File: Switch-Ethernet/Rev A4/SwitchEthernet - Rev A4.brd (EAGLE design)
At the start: 86 x 90 mm, 118 parts, among them J1 22-05-7028-02, J2 DF17(2.0)-20DP-0.5V(57), J3 DF17(4.0)-20DP-0.5V(57), J4 22-05-7058-05, P1 RB1-125BAG1A, T1 H1102FNL, T2 H1102FNL, U1 TC1264-3.3, U2 TC1264-1.8, U3 KSZ8995MA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

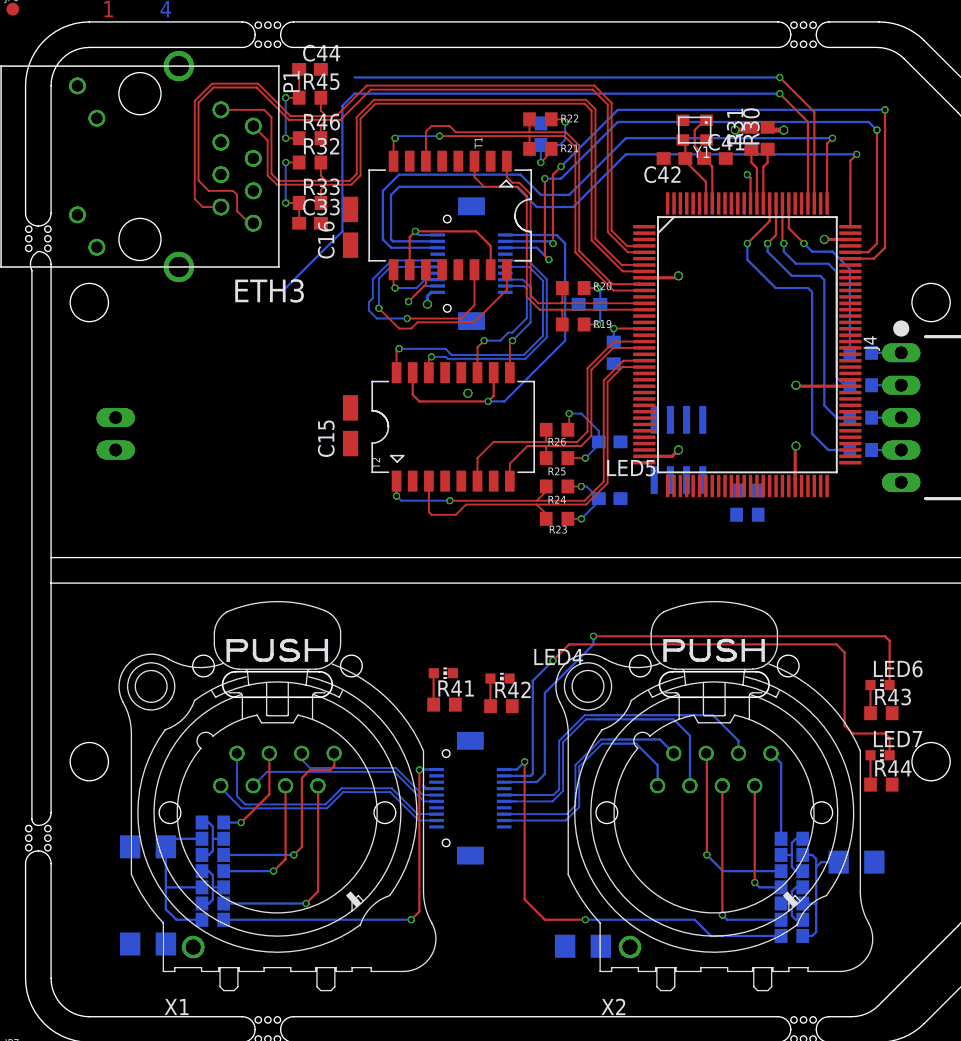
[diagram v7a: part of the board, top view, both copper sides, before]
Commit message: change position of the resistors of neutrix connectors and re-route
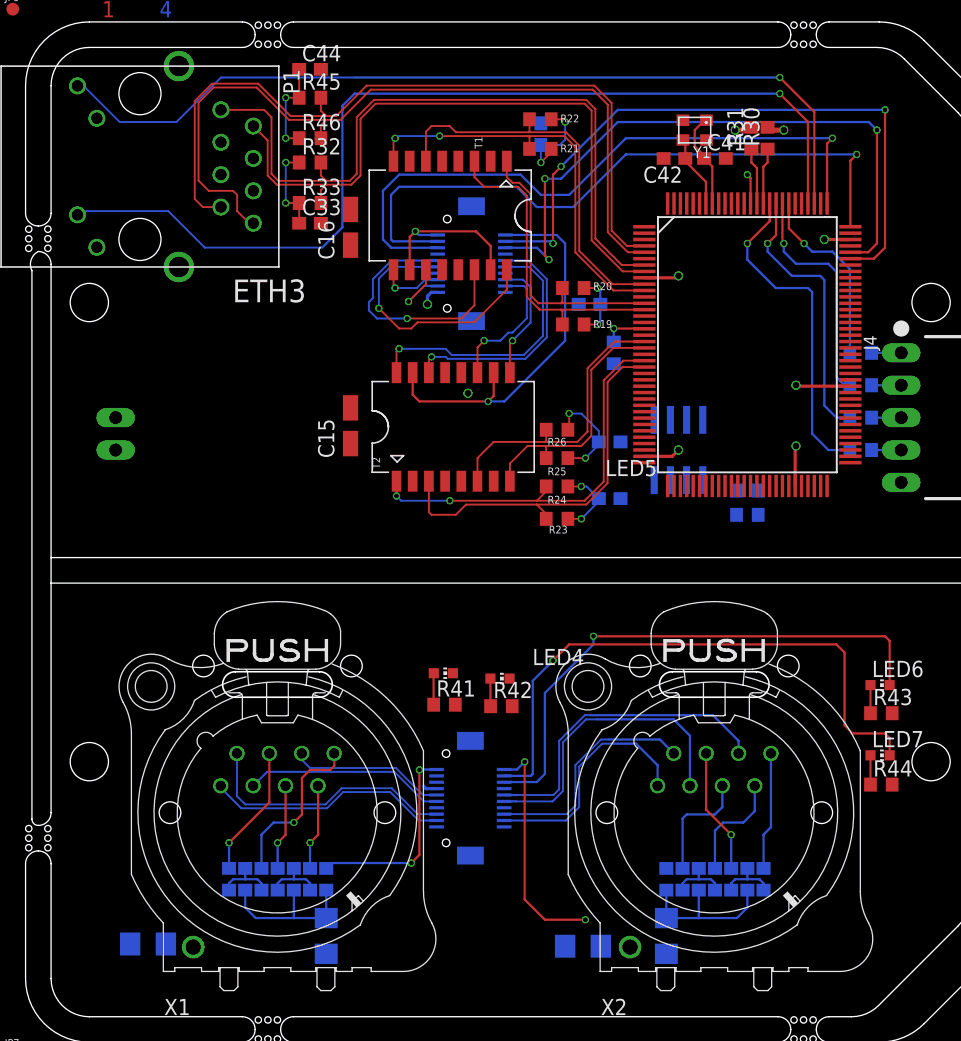
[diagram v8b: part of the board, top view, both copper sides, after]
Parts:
- moved C11 16.0 mm to (55.2, 13.3), turned to 270 degrees
- moved C12 15.6 mm to (28.6, 13.3), turned to 270 degrees
- moved R13 10.8 mm to (55.2, 17.8), turned to 90 degrees
- moved R6 9.44 mm to (28.6, 17.8), turned to 90 degrees
- moved R14 9.14 mm to (56.5, 17.8), turned to 90 degrees
- moved R8 7.85 mm to (27.3, 17.8), turned to 90 degrees
- moved R15 7.55 mm to (57.8, 17.8), turned to 90 degrees
- moved R18 6.38 mm to (26.0, 17.8), turned to 90 degrees
- moved R12 6.07 mm to (59.1, 17.8), turned to 90 degrees
- moved R17 5.12 mm to (24.8, 17.8), turned to 90 degrees
- moved R16 4.80 mm to (60.3, 17.8), turned to 90 degrees
- moved R11 4.62 mm to (21.0, 17.8), turned to 90 degrees
- moved R5 4.26 mm to (23.5, 17.8), turned to 90 degrees
- moved R10 4.07 mm to (22.2, 17.8), turned to 90 degrees
- moved R7 3.98 mm to (61.6, 17.8), turned to 90 degrees
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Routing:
- net L3-2: track 44.3 -> 68.7 mm
- net L3-1: track 60.3 -> 76.5 mm
- net CT_2: track 64.8 -> 49.0 mm
- net CT_1: track 41.4 -> 29.1 mm
- net N$9: track 16.1 -> 6.75 mm
- net N$18: track 14.9 -> 9.07 mm, vias 1 -> 0
- net N$15: track 14.3 -> 9.83 mm
- net N$11: track 11.0 -> 6.74 mm
- net N$7: track 7.71 -> 10.3 mm
- net N$8: track 15.7 -> 13.3 mm
- net N$5: track 7.04 -> 9.32 mm
- net N$32: track 14.0 -> 12.5 mm
- net N$13: track 11.1 -> 12.5 mm
- net N$12: track 9.81 -> 8.70 mm, vias 1 -> 0
